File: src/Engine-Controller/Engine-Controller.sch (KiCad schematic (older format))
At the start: 16 parts, among them J1 Jumper_NO, U1 STM32L443VCT6

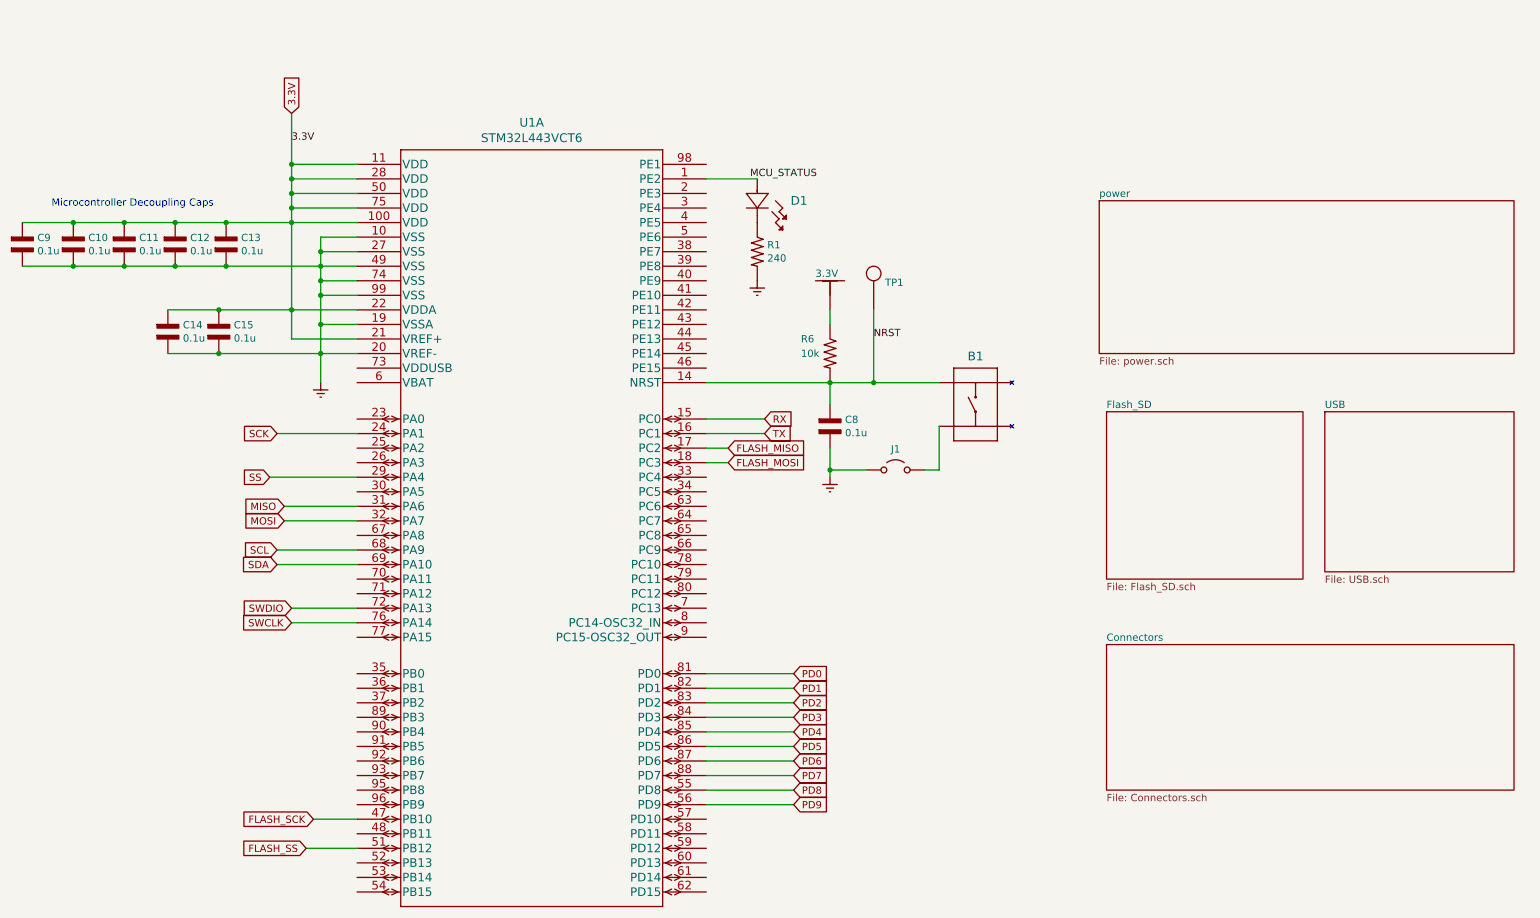
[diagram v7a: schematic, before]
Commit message: Added ADC Inputs
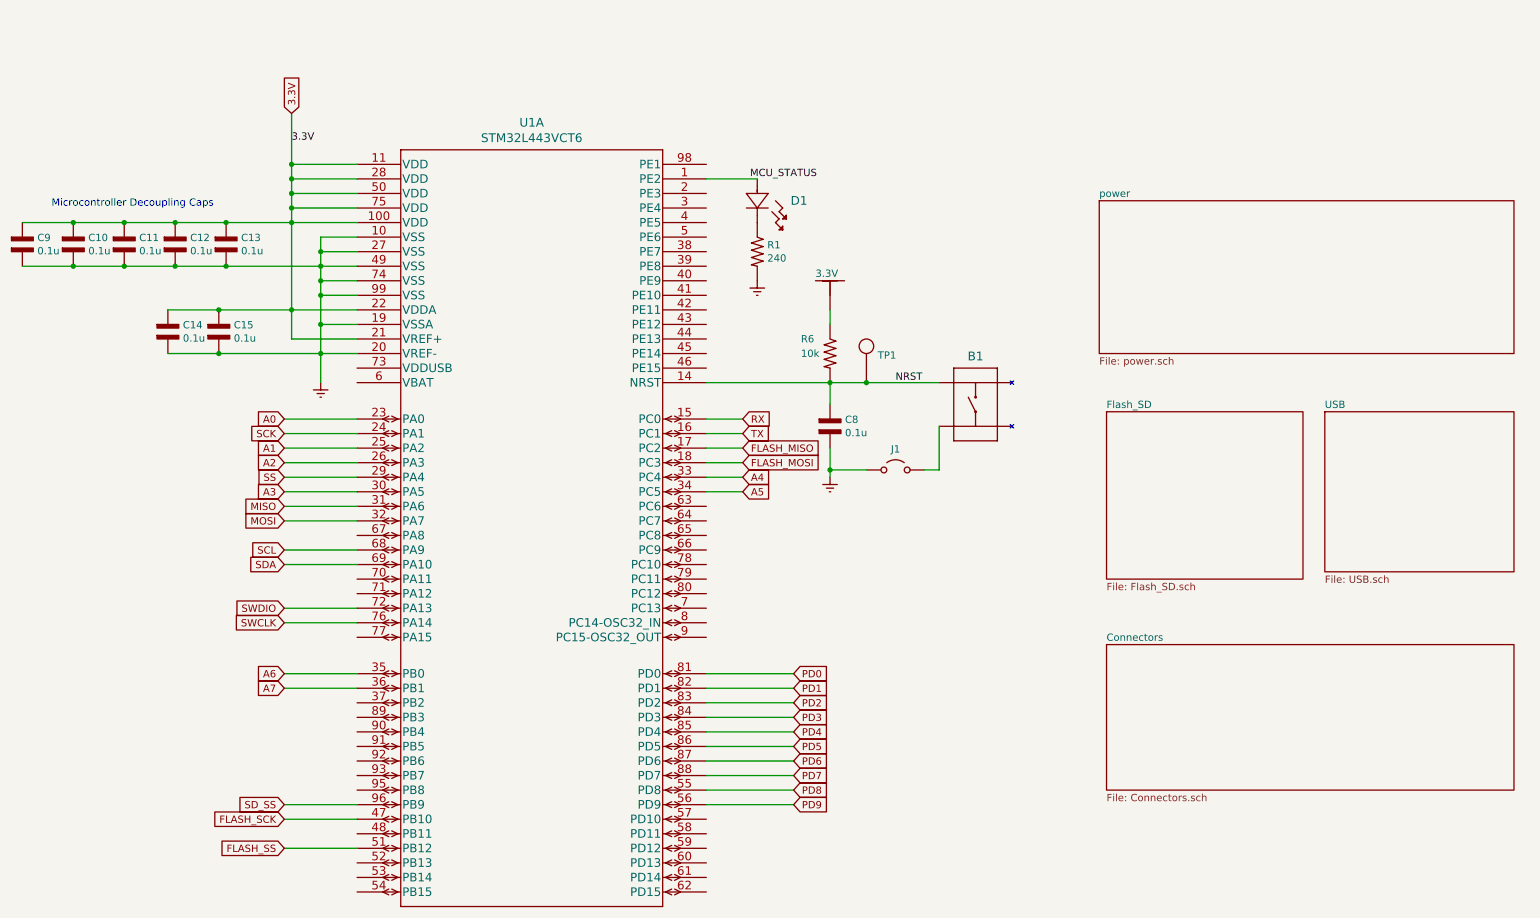
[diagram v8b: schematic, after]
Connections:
- net A0: now reaches U1.23 (PA0)
- net A1: now reaches U1.25 (PA2)
- net A2: now reaches U1.26 (PA3)
- net A3: now reaches U1.30 (PA5)
- net A4: now reaches U1.33 (PC4)
- net A5: now reaches U1.34 (PC5)
- net A6: now reaches U1.35 (PB0)
- net A7: now reaches U1.36 (PB1)
- net SD_SS: now reaches U1.96 (PB9)
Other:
- moved on the sheet: TP1
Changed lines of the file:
@@
 F1 "Connectors.sch" 50
 $EndSheet
-Text GLabel 5800 3350 2    50   Input ~ 0
+Text GLabel 5650 3350 2    50   Input ~ 0
 RX
-Text GLabel 5800 3450 2    50   Input ~ 0
+Text GLabel 5650 3450 2    50   Input ~ 0
 TX
 Text GLabel 2500 4050 0    50   Input ~ 0
@@
 Text GLabel 2500 3950 0    50   Input ~ 0
 MISO
-Text GLabel 2450 3450 0    50   Input ~ 0
+Text GLabel 2500 3450 0    50   Input ~ 0
 SCK
-Text GLabel 2450 4350 0    50   Input ~ 0
+Text GLabel 2500 4350 0    50   Input ~ 0
 SDA
-Text GLabel 2450 4250 0    50   Input ~ 0
+Text GLabel 2500 4250 0    50   Input ~ 0
 SCL
-Text GLabel 2400 3750 0    50   Input ~ 0
+Text GLabel 2500 3750 0    50   Input ~ 0
 SS
 Wire Wire Line
@@
 	3000 4050 2500 4050
 Wire Wire Line
-	2450 3450 3000 3450
-Wire Wire Line
-	2400 3750 3000 3750
-Wire Wire Line
-	2450 4250 3000 4250
-Wire Wire Line
-	3000 4350 2450 4350
+	2500 3450 3000 3450
+Wire Wire Line
+	2500 3750 3000 3750
+Wire Wire Line
+	2500 4250 3000 4250
+Wire Wire Line
+	3000 4350 2500 4350
 Text GLabel 2550 1250 1    50   Input ~ 0
 3.3V
@@
 	2750 2100 2750 2200
 Connection ~ 2750 2200
-Text GLabel 2550 4750 0    50   Input ~ 0
+Text GLabel 2500 4750 0    50   Input ~ 0
 SWCLK
-Text GLabel 2550 4650 0    50   Input ~ 0
+Text GLabel 2500 4650 0    50   Input ~ 0
 SWDIO
 Wire Wire Line
-	3000 4650 2550 4650
-Wire Wire Line
-	3000 4750 2550 4750
+	3000 4650 2500 4650
+Wire Wire Line
+	3000 4750 2500 4750
 Text GLabel 6000 5100 2    50   Input ~ 0
 PD0
@@
 L Engine-Controller:TP TP1
 U 1 1 60E1CD7C
-P 6550 2600
-F 0 "TP1" H 6628 2788 50  0000 L CNN
-F 1 "TPNRST" H 6628 2697 50  0001 L CNN
-F 2 "Engine-Controller:TP" H 6550 2600 50  0001 C CNN
-F 3 "" H 6550 2600 50  0001 C CNN
-	1    6550 2600
-	1    0    0    -1
-$EndComp
-Wire Wire Line
-	5400 3350 5800 3350
-Wire Wire Line
-	5800 3450 5400 3450
+P 6500 3100
+F 0 "TP1" H 6578 3288 50  0000 L CNN
+F 1 "TPNRST" H 6578 3197 50  0001 L CNN
+F 2 "Engine-Controller:TP" H 6500 3100 50  0001 C CNN
+F 3 "" H 6500 3100 50  0001 C CNN
+	1    6500 3100
+	1    0    0    -1
+$EndComp
+Wire Wire Line
+	5400 3350 5650 3350
+Wire Wire Line
+	5650 3450 5400 3450
 $Comp
 L power:Earth #PWR0102
@@
 Wire Wire Line
 	5400 3100 6250 3100
-Wire Wire Line
-	6250 3100 6550 3100
-Wire Wire Line
-	6550 2600 6550 3100
-Connection ~ 6550 3100
 $Comp
 L Engine-Controller:CAP_0603 C10
@@
 Text Notes 900  1900 0    50   ~ 0
 Microcontroller Decoupling Caps
-Text Label 6550 2800 0    50   ~ 0
+Text Label 6700 3100 0    50   ~ 0
 NRST
 Wire Wire Line
@@
 	7000 3700 7000 3400
 Wire Wire Line
-	6550 3100 7000 3100
-Wire Wire Line
 	6900 3700 7000 3700
 Wire Wire Line
@@
 Wire Wire Line
 	2050 2900 2750 2900
-Text GLabel 2700 6100 0    50   Input ~ 0
+Text GLabel 2500 6100 0    50   Input ~ 0
 FLASH_SCK
 Wire Wire Line
-	3000 6100 2700 6100
-Text GLabel 5550 3550 2    50   Input ~ 0
+	3000 6100 2500 6100
+Text GLabel 5650 3550 2    50   Input ~ 0
 FLASH_MISO
 Wire Wire Line
-	5550 3550 5400 3550
-Text GLabel 5550 3650 2    50   Input ~ 0
+	5650 3550 5400 3550
+Text GLabel 5650 3650 2    50   Input ~ 0
 FLASH_MOSI
 Wire Wire Line
-	5550 3650 5400 3650
-Text GLabel 2650 6300 0    50   Input ~ 0
+	5650 3650 5400 3650
+Text GLabel 2500 6300 0    50   Input ~ 0
 FLASH_SS
 Wire Wire Line
-	3000 6300 2650 6300
+	3000 6300 2500 6300
 $Sheet
 S 8150 3300 1350 1150
@@
 Text Label 5700 1700 0    50   ~ 0
 MCU_STATUS
+Wire Wire Line
+	6250 3100 6500 3100
+Connection ~ 6500 3100
+Wire Wire Line
+	6500 3100 7000 3100
+Text GLabel 2500 3350 0    50   Input ~ 0
+A0
+Text GLabel 2500 3550 0    50   Input ~ 0
+A1
+Text GLabel 2500 3650 0    50   Input ~ 0
+A2
+Text GLabel 2500 3850 0    50   Input ~ 0
+A3
+Text GLabel 5650 3750 2    50   Input ~ 0
+A4
+Text GLabel 5650 3850 2    50   Input ~ 0
+A5
+Text GLabel 2500 5100 0    50   Input ~ 0
+A6
+Text GLabel 2500 5200 0    50   Input ~ 0
+A7
+Text GLabel 2500 6000 0    50   Input ~ 0
+SD_SS
+Wire Wire Line
+	3000 6000 2500 6000
+Wire Wire Line
+	3000 3350 2500 3350
+Wire Wire Line
+	3000 3550 2500 3550
+Wire Wire Line
+	3000 3650 2500 3650
+Wire Wire Line
+	3000 3850 2500 3850
+Wire Wire Line
+	5650 3750 5400 3750
+Wire Wire Line
+	5650 3850 5400 3850
+Wire Wire Line
+	3000 5100 2500 5100
+Wire Wire Line
+	2500 5200 3000 5200
 $EndSCHEMATC
